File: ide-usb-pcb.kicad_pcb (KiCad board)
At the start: 2 copper layers, 37 parts, among them J1 Conn_02x20_Odd_Even, J10 Conn_01x02_Male, J2 STM32F4_Discovery_Header, J3 Screw_Terminal_01x02, J4 USB_B, J5 Conn_01x01_Male, J6 Conn_01x03_Male, J7 Conn_01x02_Male, J8 Conn_01x01_Male, J9 Conn_01x01_Male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

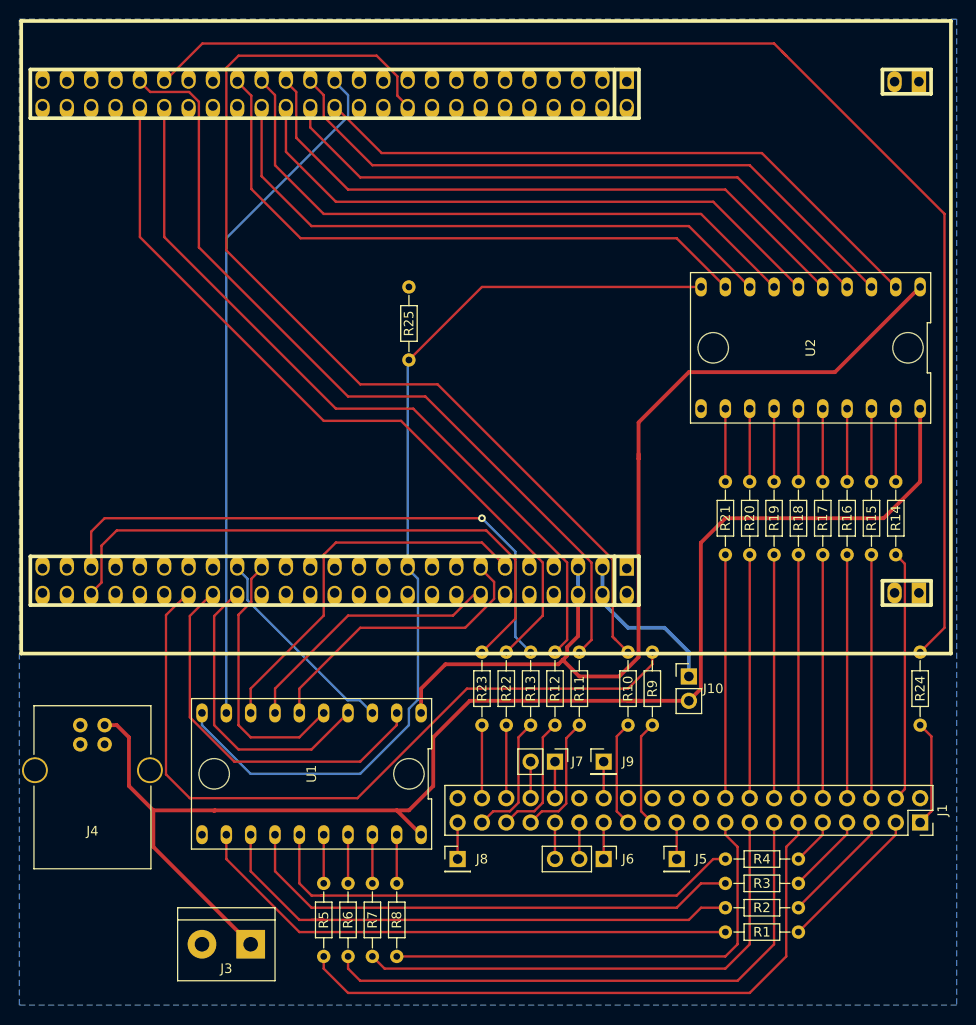
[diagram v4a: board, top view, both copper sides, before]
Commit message: Minor improvements in component placing and traces
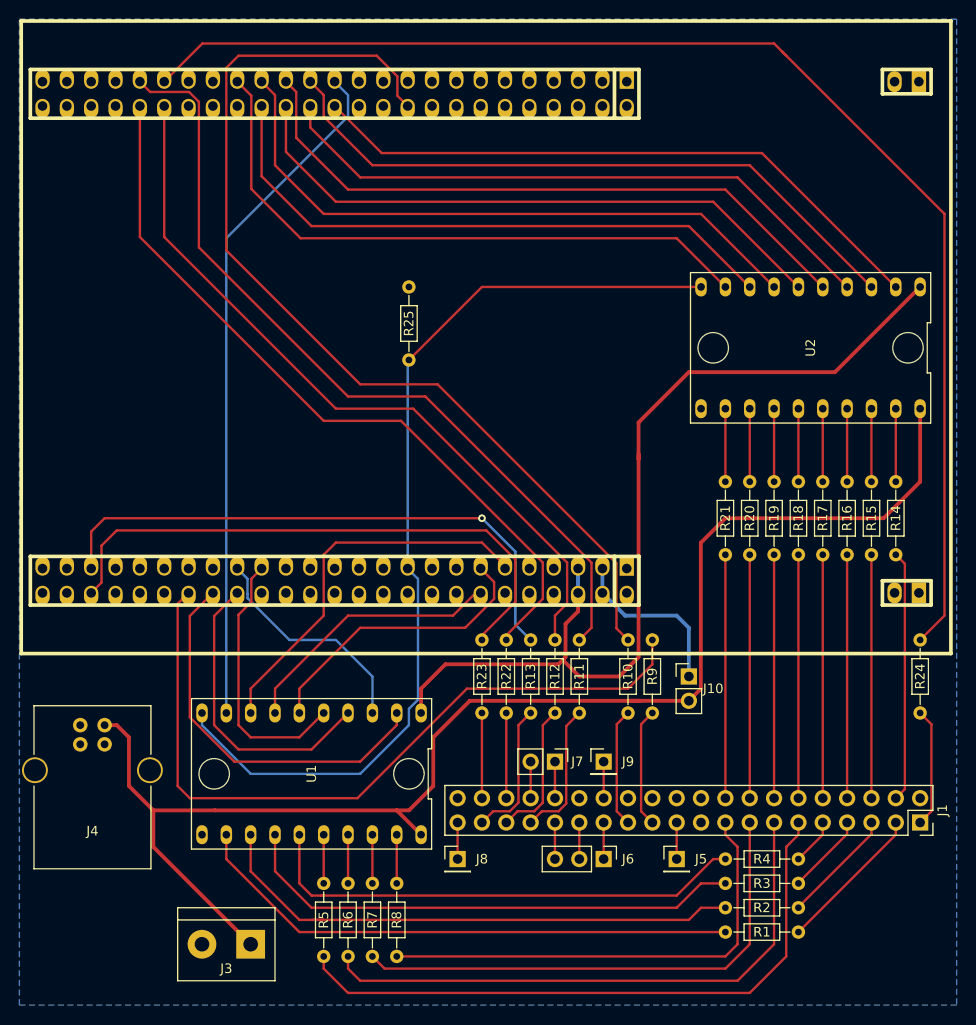
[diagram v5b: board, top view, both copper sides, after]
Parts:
- moved R10 1.27 mm to (96.5, 115.6)
- moved R11 1.27 mm to (91.4, 115.6)
- moved R12 1.27 mm to (88.9, 115.6)
- moved R13 1.27 mm to (86.4, 115.6)
- moved R24 1.27 mm to (127.0, 115.6)
- moved R9 1.27 mm to (99.1, 115.6)
- moved R22 1.27 mm to (83.8, 108.0)
- moved R23 1.27 mm to (81.3, 108.0)
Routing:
- net /DD1A: track 21.7 -> 23.8 mm
- net /+5VBOARD: track 17.2 -> 19.1 mm
- net /DIOR: track 106.3 -> 104.7 mm
- net Net-(J1-Pad38): track 7.62 -> 8.89 mm
- net Net-(J1-Pad36): track 7.62 -> 8.89 mm
- net /DA0: track 79.6 -> 78.4 mm
- net Net-(J1-Pad35): track 13.3 -> 14.6 mm
- net Net-(J1-Pad23): track 11.1 -> 12.4 mm
- net Net-(J1-Pad1): track 11.1 -> 12.4 mm
- net Net-(J1-Pad37): track 13.3 -> 14.6 mm
- net Net-(J1-Pad33): track 13.3 -> 14.6 mm
- net Net-(J1-Pad25): track 11.1 -> 12.4 mm
- net /DA2: track 80.7 -> 79.4 mm
- net /CS1: track 61.6 -> 60.3 mm
- net /CS0: track 61.4 -> 60.1 mm
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
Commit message: More small adjustments (silkscreen, move J3 & J4)
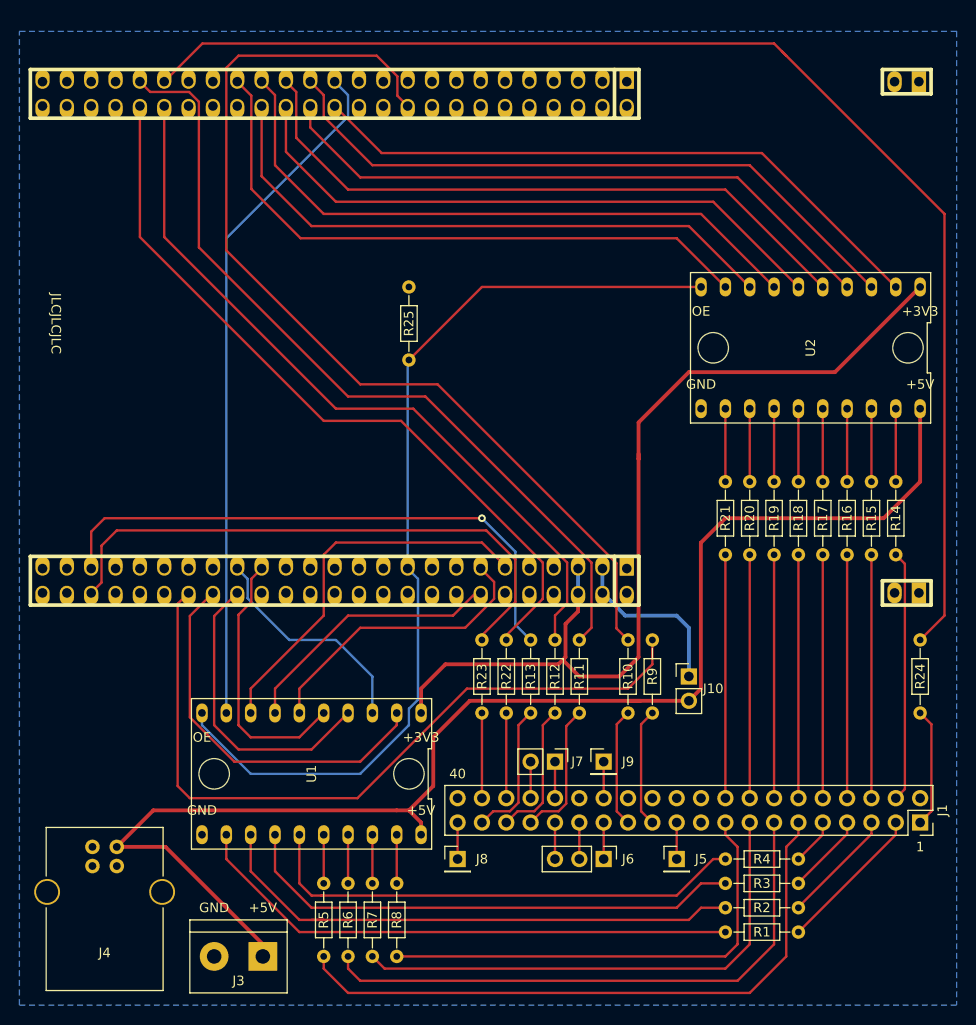
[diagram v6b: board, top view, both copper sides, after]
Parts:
- moved J4 12.8 mm to (43.2, 129.5)
- moved J3 1.80 mm to (58.4, 141.0)
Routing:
- net +5V: track 149.8 -> 144.2 mm
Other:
- board text added: "+3V3"
- board text added: "+5V"
- board text added: "1"
- board text added: "40"
- board text added: "GND"
- board text added: "JLCJLCJLC"
- board text added: "OE"

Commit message: Export Gergebs with JLC guidelines
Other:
- board outline added: 97.8 x 101.6 mm

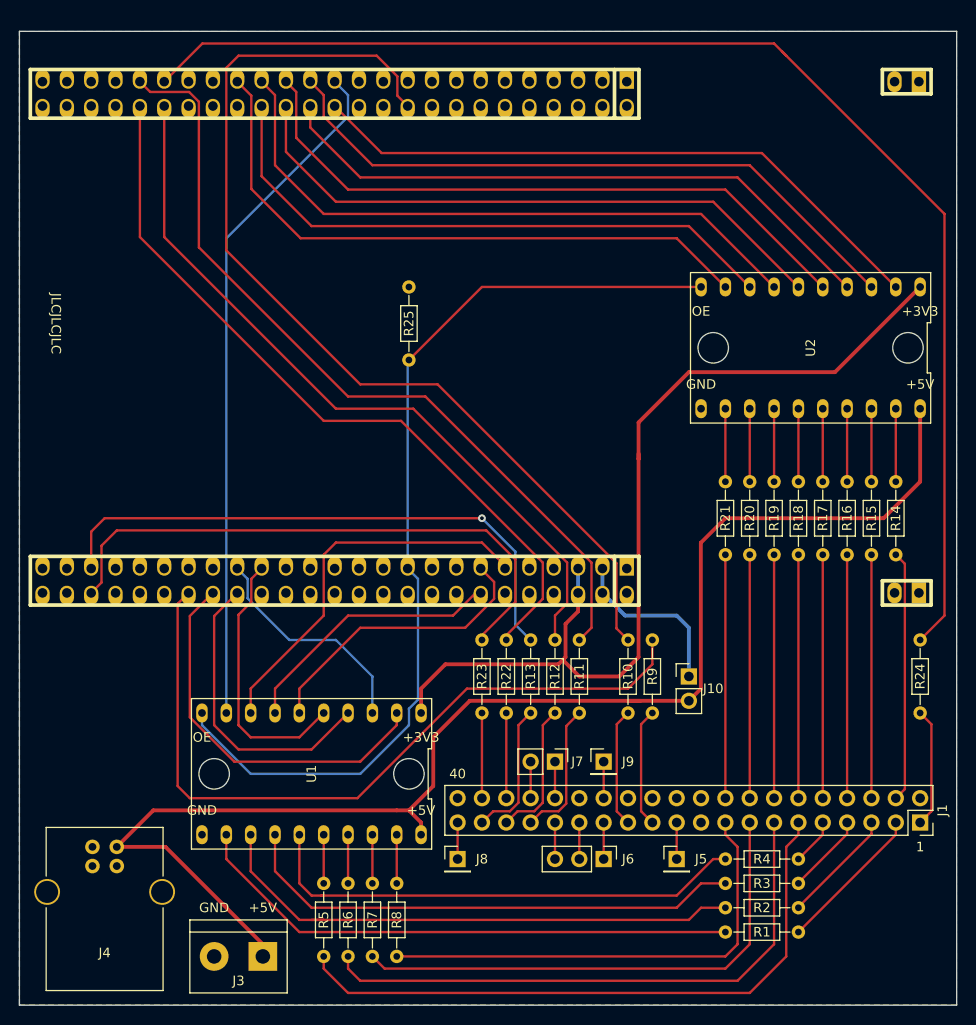
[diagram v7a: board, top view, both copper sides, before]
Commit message: Increase hole and pad size for TXS0108E breakout
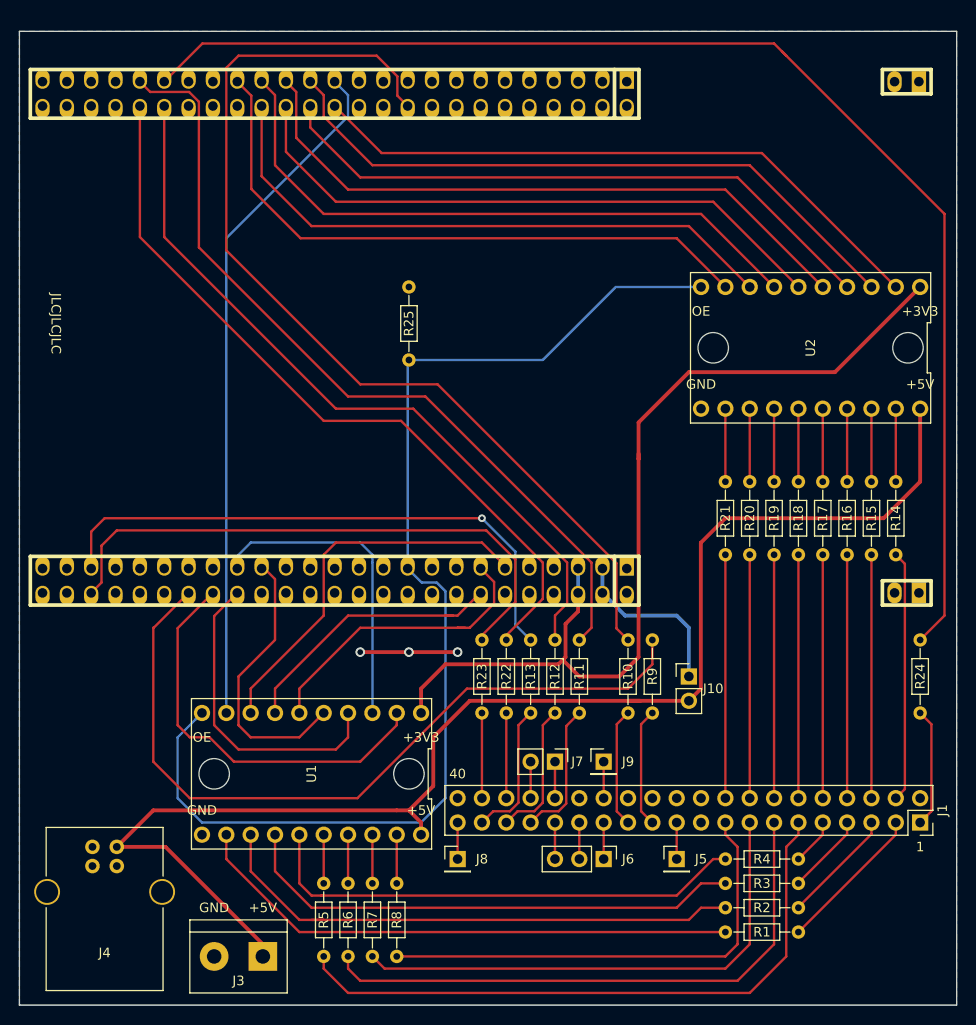
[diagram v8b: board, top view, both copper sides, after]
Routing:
- net /OE: track 99.7 -> 122.9 mm
- net GND: track 0.00 -> 10.2 mm, vias 0 -> 3
- net /DD1A: track 23.8 -> 33.0 mm
- net /DD0A: track 40.3 -> 42.6 mm
- net /DIOW: track 79.0 -> 81.1 mm
- net /DD2A: track 31.4 -> 32.9 mm
- net /DD3A: track 27.8 -> 29.1 mm
- net /DD5A: track 28.1 -> 29.4 mm
- net /DD4A: track 30.5 -> 31.6 mm
